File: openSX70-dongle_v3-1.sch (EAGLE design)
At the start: 26 parts

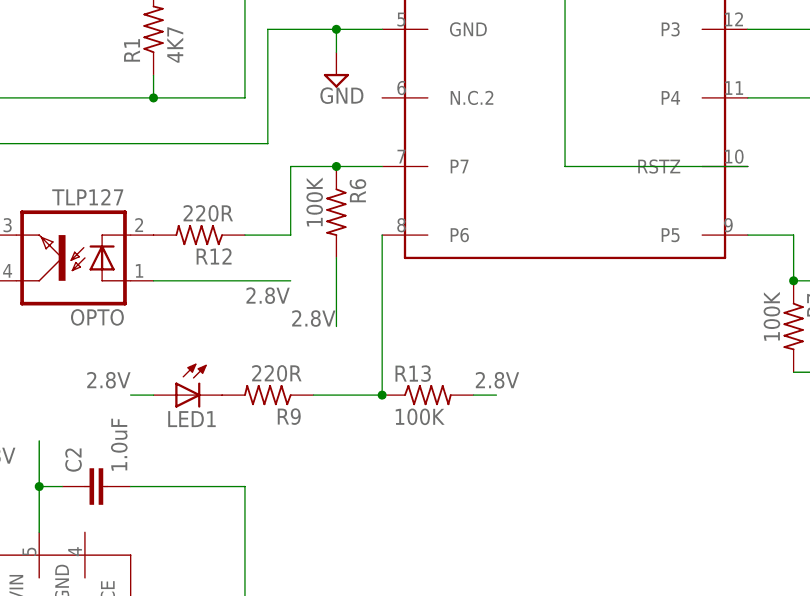
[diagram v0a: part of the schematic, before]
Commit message: Added a 2.8V regulator needed to work with the 2.5V arduino. Removed R13 and R6 (pullup resistors to VCC for LED and opto), since they were not needed.
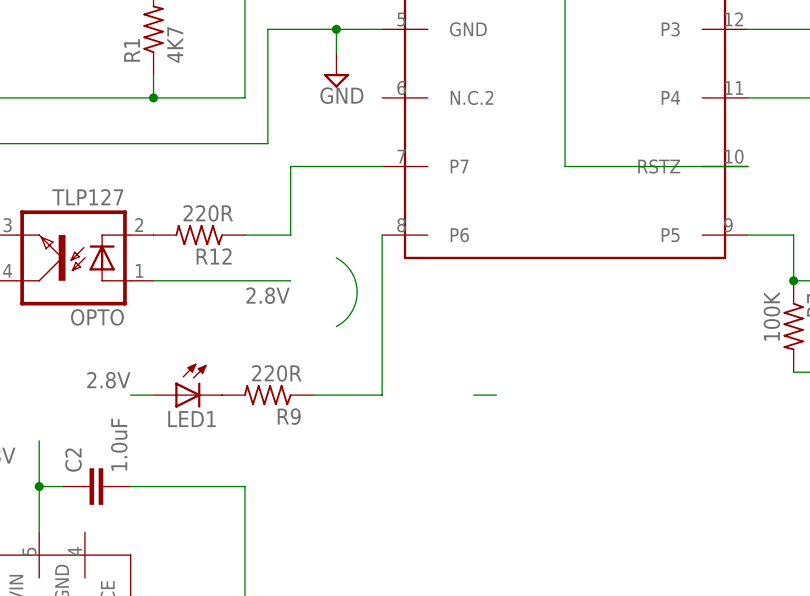
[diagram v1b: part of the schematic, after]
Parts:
- removed R13, R6: 100K, rcl:R-US_M0805
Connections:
- net 2.8V: no longer R13.2, R6.2
- net N$11: no longer R6.1
- net N$8: no longer R13.1
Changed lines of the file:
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@@
 <part name="R4" library="rcl" library_urn="urn:adsk.eagle:library:334" deviceset="R-US_" device="M0805" package3d_urn="urn:adsk.eagle:package:23556/1" value="100K"/>
 <part name="R5" library="rcl" library_urn="urn:adsk.eagle:library:334" deviceset="R-US_" device="M0805" package3d_urn="urn:adsk.eagle:package:23556/1" value="100K"/>
-<part name="R6" library="rcl" library_urn="urn:adsk.eagle:library:334" deviceset="R-US_" device="M0805" package3d_urn="urn:adsk.eagle:package:23556/1" value="100K"/>
 <part name="R7" library="rcl" library_urn="urn:adsk.eagle:library:334" deviceset="R-US_" device="M0805" package3d_urn="urn:adsk.eagle:package:23556/1" value="100K"/>
 <part name="R8" library="rcl" library_urn="urn:adsk.eagle:library:334" deviceset="R-US_" device="M0805" package3d_urn="urn:adsk.eagle:package:23556/1" value="100K"/>
@@
 <part name="OPTO" library="openSX70" deviceset="TLP127" device="" value="TLP127"/>
 <part name="R12" library="rcl" library_urn="urn:adsk.eagle:library:334" deviceset="R-US_" device="M0805" package3d_urn="urn:adsk.eagle:package:23556/1" value="220R"/>
-<part name="R13" library="rcl" library_urn="urn:adsk.eagle:library:334" deviceset="R-US_" device="M0805" package3d_urn="urn:adsk.eagle:package:23556/1" value="100K"/>
 <part name="PC-FLASH" library="SparkFun-Connectors" deviceset="AUDIO_JACK_3.5MM" device="_PTH"/>
 <part name="FRAME1" library="frames" library_urn="urn:adsk.eagle:library:229" deviceset="DINA4_L" device=""/>
@@
 <instance part="R4" gate="G$1" x="208.28" y="104.14" rot="R180"/>
 <instance part="R5" gate="G$1" x="208.28" y="88.9" rot="R180"/>
-<instance part="R6" gate="G$1" x="109.22" y="55.88" rot="R270"/>
 <instance part="R7" gate="G$1" x="160.02" y="43.18" rot="R270"/>
 <instance part="R8" gate="G$1" x="172.72" y="63.5" rot="R270"/>
@@
 <instance part="OPTO" gate="G$1" x="78.74" y="50.8" rot="R180"/>
 <instance part="R12" gate="G$1" x="93.98" y="53.34" rot="R180"/>
-<instance part="R13" gate="G$1" x="119.38" y="35.56"/>
 <instance part="PC-FLASH" gate="G$1" x="48.26" y="50.8"/>
 <instance part="FRAME1" gate="G$1" x="-7.62" y="-15.24"/>
@@
 <wire x1="104.14" y1="53.34" x2="104.14" y2="60.96" width="0.1524" layer="91"/>
 <pinref part="DS2408" gate="G$1" pin="P7"/>
-<wire x1="104.14" y1="60.96" x2="109.22" y2="60.96" width="0.1524" layer="91"/>
-<pinref part="R6" gate="G$1" pin="1"/>
-<wire x1="109.22" y1="60.96" x2="114.3" y2="60.96" width="0.1524" layer="91"/>
-<junction x="109.22" y="60.96"/>
+<wire x1="104.14" y1="60.96" x2="114.3" y2="60.96" width="0.1524" layer="91"/>
 </segment>
 </net>
@@
 <pinref part="R9" gate="G$1" pin="1"/>
 <wire x1="114.3" y1="35.56" x2="106.68" y2="35.56" width="0.1524" layer="91"/>
-<pinref part="R13" gate="G$1" pin="1"/>
-<junction x="114.3" y="35.56"/>
 </segment>
 </net>
@@
 </segment>
 <segment>
-<pinref part="R13" gate="G$1" pin="2"/>
 <wire x1="124.46" y1="35.56" x2="127" y2="35.56" width="0.1524" layer="91"/>
-<label x="129.54" y="38.1" size="1.778" layer="95" rot="R180"/>
 </segment>
 <segment>
@@
 </segment>
 <segment>
-<pinref part="R6" gate="G$1" pin="2"/>
-<wire x1="109.22" y1="50.8" x2="109.22" y2="43.18" width="0.1524" layer="91"/>
-<label x="104.14" y="43.18" size="1.778" layer="95"/>
-</segment>
-</net>
+<wire x1="109.22" y1="50.8" x2="109.22" y2="43.18" width="0.1524" layer="91" curve="-124.850897"/>
+</segment>
+</net>

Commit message: changes
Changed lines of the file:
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@@
-</segment>
-<segment>
-<wire x1="124.46" y1="35.56" x2="127" y2="35.56" width="0.1524" layer="91"/>
 </segment>
 <segment>
@@
 <label x="195.58" y="48.26" size="1.778" layer="95"/>
 </segment>
-<segment>
-<wire x1="109.22" y1="50.8" x2="109.22" y2="43.18" width="0.1524" layer="91" curve="-124.850897"/>
-</segment>
 </net>
